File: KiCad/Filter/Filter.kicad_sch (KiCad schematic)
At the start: 37 parts, among them J1 Screw_Terminal_01x03, J2 Screw_Terminal_01x03, U1 TL074

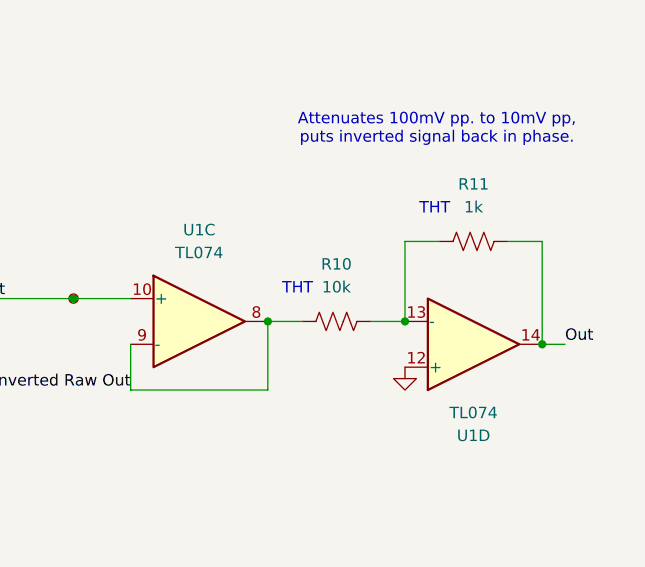
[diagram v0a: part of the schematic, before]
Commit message: added graphics to some boards
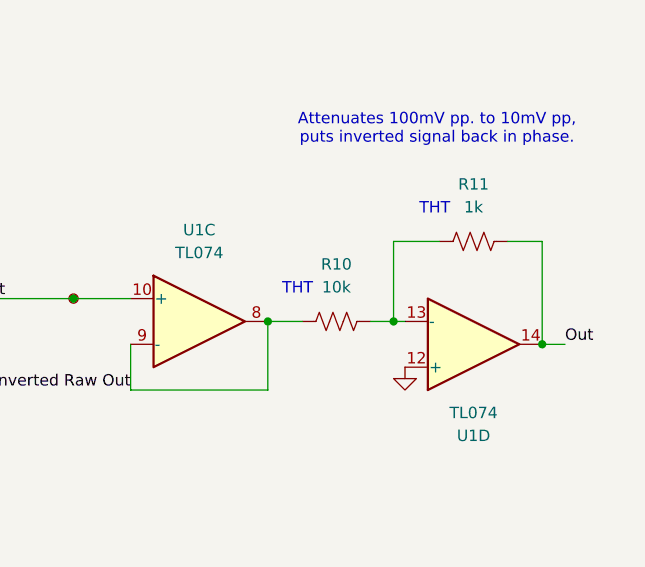
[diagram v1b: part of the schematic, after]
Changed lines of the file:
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@@
-	)
-	(junction
-		(at 185.42 66.04)
-		(diameter 0)
-		(color 0 0 0 0)
 	)
 	(junction
@@
 	)
 	(junction
+		(at 184.15 66.04)
+		(diameter 0)
+		(color 0 0 0 0)
+	)
+	(junction
 		(at 148.59 63.5)
 		(diameter 0)
@@
 	(wire
 		(pts
-			(xy 185.42 57.15) (xy 189.23 57.15)
+			(xy 184.15 57.15) (xy 189.23 57.15)
 		)
 		(stroke
@@
 	(wire
 		(pts
-			(xy 185.42 66.04) (xy 185.42 57.15)
+			(xy 184.15 66.04) (xy 184.15 57.15)
 		)
 		(stroke
@@
 	(wire
 		(pts
-			(xy 181.61 66.04) (xy 185.42 66.04)
+			(xy 181.61 66.04) (xy 184.15 66.04)
 		)
 		(stroke
@@
 		)
 		(stroke
+			(width 0)
+			(type default)
+		)
+	)
+	(wire
+		(pts
+			(xy 184.15 66.04) (xy 185.42 66.04)
+		)
+		(stroke

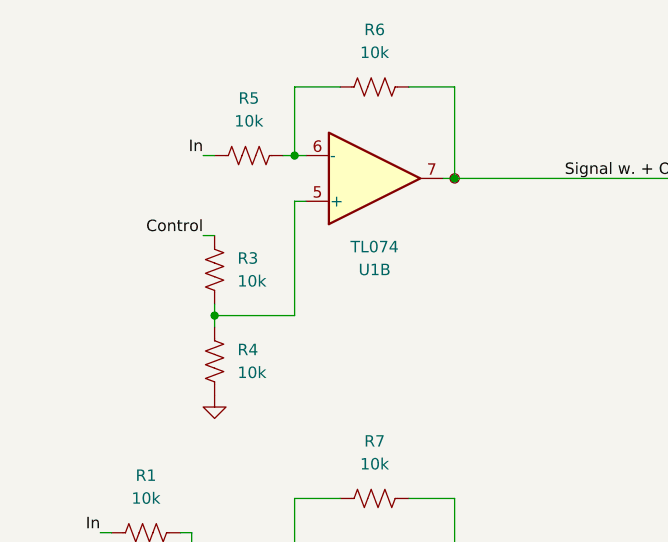
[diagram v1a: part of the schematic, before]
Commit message: preparation to merge project back into one board
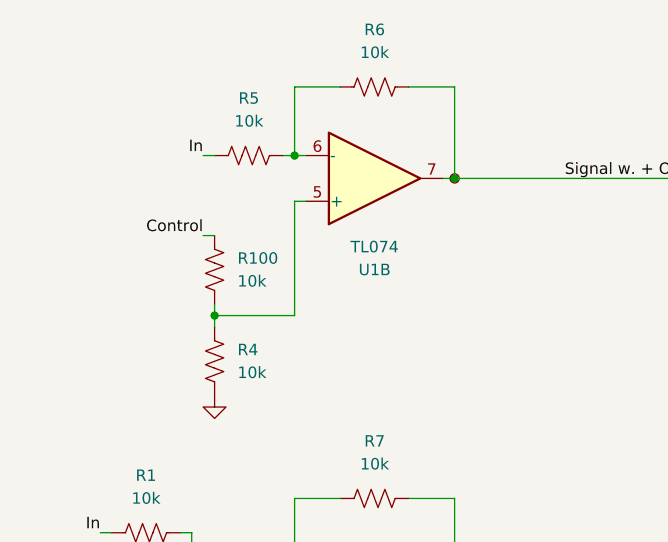
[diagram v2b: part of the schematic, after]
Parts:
- renumbered R3 to R100
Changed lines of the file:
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@@
 		(dnp no)
 		(fields_autoplaced yes)
-		(property "Reference" "R3"
+		(property "Reference" "R100"
 			(at 41.91 48.2599 0)
 			(show_name no)
@@
 			(project "Filter"
 				(path "/d0463ce5-c32c-4d9a-94ac-2a0e117a03ce"
-					(reference "R3")
+					(reference "R100")
 					(unit 1)
 				)

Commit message: merged project into one combined board (excluding the buttons)
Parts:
- renumbered C4 to C10, C5 to C11, C6 to C12, C1 to C8, C3 to C9, D6 to D10, D1 to D5, D2 to D6, D3 to D7, D4 to D8, D5 to D9, H1 to H5, H2 to H6, H4 to H7, H3 to H8, J1 to J3, J2 to J4, R1 to R11, R2 to R12, R100 to R13, R4 to R14, R5 to R15, R6 to R16, R7 to R17, R12 to R18, R8 to R19, R9 to R20, R10 to R21, R11 to R22, TP5 to TP10, TP6 to TP11, TP7 to TP12, TP1 to TP6, TP2 to TP7, TP3 to TP8, TP4 to TP9, U1 to U3
